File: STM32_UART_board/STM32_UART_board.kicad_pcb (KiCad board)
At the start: 2 copper layers, 47.5 x 42 mm, 33 parts, among them J1 SWD, J2 Scooter, Q1 AO4612_C4748739, SW1 SW_Push, SW2 SW_Push, U1 BAS70-05, U2 LM2574HVM-5, U3 AZ1117-3.3, U4 STM32C011F6Px

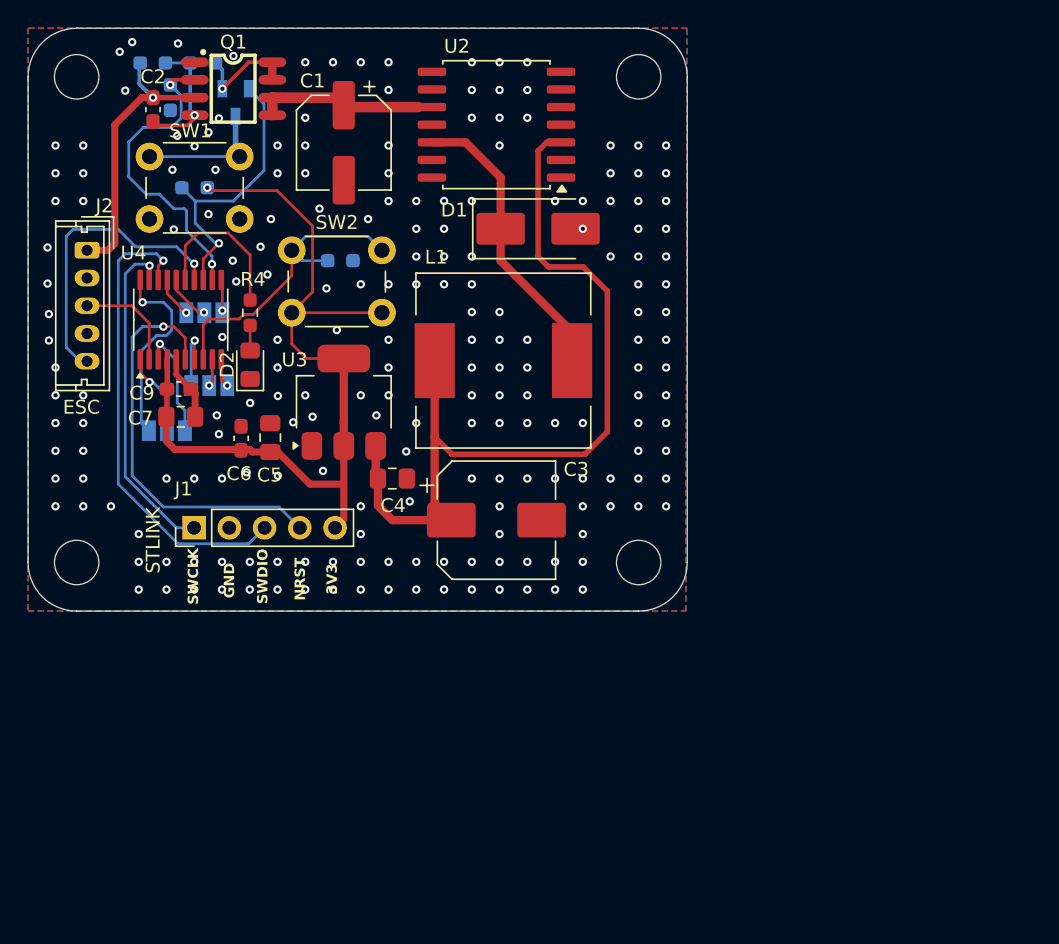
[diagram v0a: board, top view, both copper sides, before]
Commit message: PCB with swapped RX TX | initial code fot STM32C011
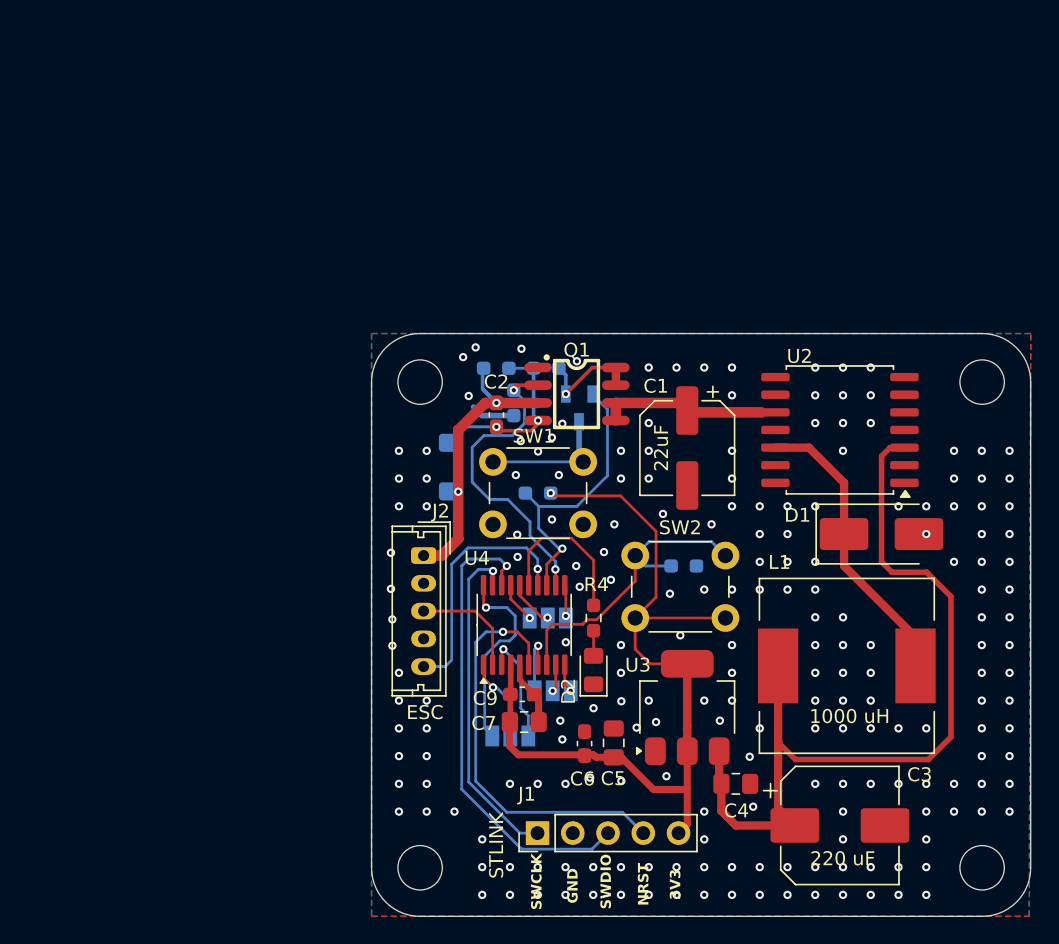
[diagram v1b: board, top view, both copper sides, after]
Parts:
- added D3: BZV55B15, Diode_SMD:D_MiniMELF, B.Cu at (94.0, 74.1)
- L1: value 680 uH -> 1000 uH
- moved C1 33.1 mm to (111.0, 72.8)
- moved C2 33.1 mm to (97.2, 70.4)
- moved C3 33.1 mm to (122.0, 100.0)
- moved C4 33.1 mm to (114.5, 97.0)
- moved C5 33.1 mm to (105.7, 94.0)
- moved C6 33.1 mm to (103.6, 94.0)
- moved C7 33.1 mm to (99.2, 92.5)
- moved C9 33.1 mm to (99.1, 90.5)
- moved D1 33.1 mm to (125.0, 79.0)
- moved D2 33.1 mm to (104.2, 88.8)
- moved H1 33.1 mm to (91.8, 103.0)
- moved H2 33.1 mm to (132.2, 103.0)
- moved H3 33.1 mm to (91.8, 68.0)
- moved H4 33.1 mm to (132.2, 68.0)
- moved J1 33.1 mm to (100.2, 100.5)
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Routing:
- net BATT+: track 21.0 -> 26.9 mm, vias 1 -> 2
- net /Q1_G1: track 9.23 -> 13.0 mm, vias 1 -> 2
- net /EN: track 21.5 -> 18.0 mm
- net GND: track 4.98 -> 8.13 mm, vias 203 -> 204

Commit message: minor PCB changes
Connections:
- J2 pad 3: /PC14 -> /SCOOTER_TX
- J2 pad 4: /SCOOTER_TX -> /PC14
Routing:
- net /PC14: track 7.61 -> 6.41 mm
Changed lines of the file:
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@@
 			(layers "*.Cu" "*.Mask")
 			(remove_unused_layers no)
-			(net 17 "/PC14")
+			(net 11 "/SCOOTER_TX")
 			(pinfunction "Pin_3")
-			(pintype "passive")
+			(pintype "passive+no_connect")
 		)
 		(pad "4" thru_hole oval
@@
 			(layers "*.Cu" "*.Mask")
 			(remove_unused_layers no)
-			(net 11 "/SCOOTER_TX")
+			(net 17 "/PC14")
 			(pinfunction "Pin_4")
 			(pintype "passive")
@@
 	)
 	(segment
-		(start 95.725 84.5)
-		(end 96.975 85.75)
+		(start 96.25 86.5)
+		(end 92 86.5)
 		(width 0.2)
 		(layer "F.Cu")
@@
 	)
 	(segment
-		(start 96.975 88.3625)
-		(end 96.975 85.75)
+		(start 96.975 87.225)
+		(end 96.25 86.5)
 		(width 0.2)
 		(layer "F.Cu")
@@
 	)
 	(segment
-		(start 92.5 84.5)
-		(end 95.725 84.5)
+		(start 96.975 88.3625)
+		(end 96.975 87.225)
 		(width 0.2)
 		(layer "F.Cu")
